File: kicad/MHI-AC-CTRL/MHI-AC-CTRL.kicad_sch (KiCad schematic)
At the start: 9 parts, among them J1 Conn_01x05, J3 Conn_01x03, U1 TSR_1-2450, U2 WeMos_D1_mini, U3 LEVEL-SHIFTER-4CH

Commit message: KiCad: Fix J1 connector (#155)
This fixes the J1 connector footprint and 3D model by using
easyeda2kicad [0] to pull the data from LCSC!

Closes #111

[0]: https://github.com/uPesy/easyeda2kicad.py

Signed-off-by: Olliver Schinagl <oliver@schinagl.nl>
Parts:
- J1: footprint Connector_JST:JST_XH_B5B-XH-A_1x05_P2.50mm_Vertical -> easyeda2kicad:CONN-TH_5P-P2.50_05JQ-BT

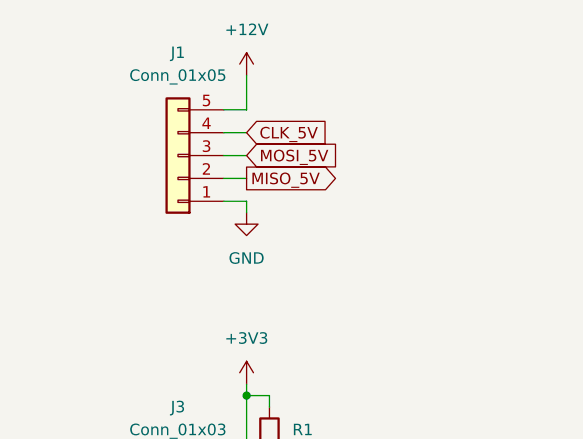
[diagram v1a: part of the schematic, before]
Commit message: Correct J1 connector pinout (#168)
Fixes #167
Regenerated PDF and gerber/drill
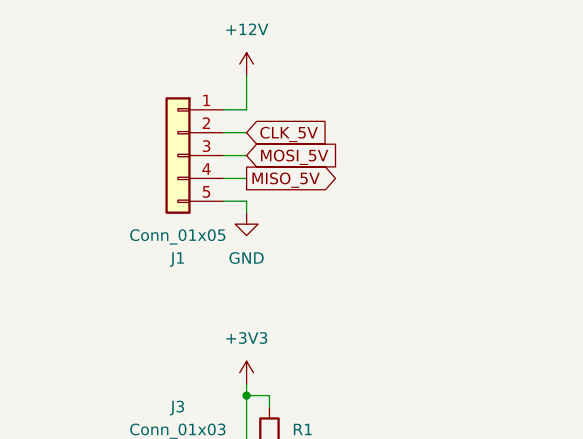
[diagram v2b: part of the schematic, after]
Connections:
- net +12V: now also J1.1 (Pin_1); no longer J1.5 (Pin_5)
- net CLK_5V: now also J1.2 (Pin_2); no longer J1.4 (Pin_4)
- net GND: now also J1.5 (Pin_5); no longer J1.1 (Pin_1)
- net MISO_5V: now also J1.4 (Pin_4); no longer J1.2 (Pin_2)
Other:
- moved on the sheet: J1
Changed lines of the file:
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@@
   (no_connect (at 111.76 54.61))
   (no_connect (at 111.76 44.45))
+  (wire (pts (xy 40.64 39.37) (xy 43.18 39.37))
+    (stroke (width 0) (type default))
+  )
   (wire (pts (xy 109.22 46.99) (xy 111.76 46.99))
     (stroke (width 0) (type default))
@@
     (stroke (width 0) (type default))
   )
+  (wire (pts (xy 40.64 44.45) (xy 43.18 44.45))
+    (stroke (width 0) (type default))
+  )
+  (wire (pts (xy 40.64 76.2) (xy 45.72 76.2))
+    (stroke (width 0) (type default))
+  )
+  (wire (pts (xy 158.75 62.23) (xy 156.21 62.23))
+    (stroke (width 0) (type default))
+  )
+  (wire (pts (xy 109.22 49.53) (xy 111.76 49.53))
+    (stroke (width 0) (type default))
+  )
+  (wire (pts (xy 109.22 54.61) (xy 111.76 54.61))
+    (stroke (width 0) (type default))
+  )
+  (wire (pts (xy 86.36 46.99) (xy 88.9 46.99))
+    (stroke (width 0) (type default))
+  )
+  (wire (pts (xy 158.75 52.07) (xy 156.21 52.07))
+    (stroke (width 0) (type default))
+  )
+  (wire (pts (xy 109.22 57.15) (xy 111.76 57.15))
+    (stroke (width 0) (type default))
+  )
+  (wire (pts (xy 31.75 111.76) (xy 31.75 110.49))
+    (stroke (width 0) (type default))
+  )
+  (wire (pts (xy 109.22 62.23) (xy 111.76 62.23))
+    (stroke (width 0) (type default))
+  )
+  (wire (pts (xy 43.18 73.66) (xy 43.18 66.04))
+    (stroke (width 0) (type default))
+  )
+  (wire (pts (xy 31.75 101.6) (xy 31.75 110.49))
+    (stroke (width 0) (type default))
+  )
+  (wire (pts (xy 40.64 73.66) (xy 43.18 73.66))
+    (stroke (width 0) (type default))
+  )
+  (wire (pts (xy 43.18 78.74) (xy 43.18 80.01))
+    (stroke (width 0) (type default))
+  )
+  (wire (pts (xy 109.22 64.77) (xy 111.76 64.77))
+    (stroke (width 0) (type default))
+  )
+  (wire (pts (xy 158.75 57.15) (xy 156.21 57.15))
+    (stroke (width 0) (type default))
+  )
+  (wire (pts (xy 38.1 119.38) (xy 38.1 120.65))
+    (stroke (width 0) (type default))
+  )
+  (wire (pts (xy 40.64 41.91) (xy 43.18 41.91))
+    (stroke (width 0) (type default))
+  )
+  (wire (pts (xy 171.45 77.47) (xy 171.45 80.01))
+    (stroke (width 0) (type default))
+  )
+  (wire (pts (xy 99.06 77.47) (xy 99.06 80.01))
+    (stroke (width 0) (type default))
+  )
+  (wire (pts (xy 40.64 78.74) (xy 43.18 78.74))
+    (stroke (width 0) (type default))
+  )
+  (wire (pts (xy 43.18 66.04) (xy 43.18 64.77))
+    (stroke (width 0) (type default))
+  )
+  (wire (pts (xy 43.18 110.49) (xy 38.1 110.49))
+    (stroke (width 0) (type default))
+  )
+  (wire (pts (xy 53.34 118.11) (xy 53.34 120.65))
+    (stroke (width 0) (type default))
+  )
+  (wire (pts (xy 45.72 66.04) (xy 43.18 66.04))
+    (stroke (width 0) (type default))
+  )
+  (wire (pts (xy 109.22 52.07) (xy 111.76 52.07))
+    (stroke (width 0) (type default))
+  )
+  (wire (pts (xy 45.72 76.2) (xy 48.26 76.2))
+    (stroke (width 0) (type default))
+  )
+  (wire (pts (xy 67.31 119.38) (xy 67.31 120.65))
+    (stroke (width 0) (type default))
+  )
+  (wire (pts (xy 109.22 59.69) (xy 111.76 59.69))
+    (stroke (width 0) (type default))
+  )
+  (wire (pts (xy 179.07 62.23) (xy 181.61 62.23))
+    (stroke (width 0) (type default))
+  )
+  (wire (pts (xy 43.18 34.29) (xy 43.18 30.48))
+    (stroke (width 0) (type default))
+  )
+  (wire (pts (xy 179.07 52.07) (xy 181.61 52.07))
+    (stroke (width 0) (type default))
+  )
+  (wire (pts (xy 166.37 77.47) (xy 166.37 80.01))
+    (stroke (width 0) (type default))
+  )
   (wire (pts (xy 40.64 34.29) (xy 43.18 34.29))
     (stroke (width 0) (type default))
   )
-  (wire (pts (xy 40.64 76.2) (xy 45.72 76.2))
-    (stroke (width 0) (type default))
-  )
-  (wire (pts (xy 158.75 62.23) (xy 156.21 62.23))
-    (stroke (width 0) (type default))
-  )
-  (wire (pts (xy 109.22 49.53) (xy 111.76 49.53))
-    (stroke (width 0) (type default))
-  )
-  (wire (pts (xy 40.64 41.91) (xy 43.18 41.91))
-    (stroke (width 0) (type default))
-  )
-  (wire (pts (xy 109.22 54.61) (xy 111.76 54.61))
-    (stroke (width 0) (type default))
-  )
-  (wire (pts (xy 86.36 46.99) (xy 88.9 46.99))
-    (stroke (width 0) (type default))
-  )
-  (wire (pts (xy 158.75 52.07) (xy 156.21 52.07))
-    (stroke (width 0) (type default))
-  )
-  (wire (pts (xy 109.22 57.15) (xy 111.76 57.15))
-    (stroke (width 0) (type default))
-  )
-  (wire (pts (xy 31.75 111.76) (xy 31.75 110.49))
-    (stroke (width 0) (type default))
-  )
-  (wire (pts (xy 109.22 62.23) (xy 111.76 62.23))
-    (stroke (width 0) (type default))
-  )
-  (wire (pts (xy 43.18 73.66) (xy 43.18 66.04))
-    (stroke (width 0) (type default))
-  )
-  (wire (pts (xy 31.75 101.6) (xy 31.75 110.49))
-    (stroke (width 0) (type default))
-  )
-  (wire (pts (xy 40.64 73.66) (xy 43.18 73.66))
-    (stroke (width 0) (type default))
-  )
-  (wire (pts (xy 43.18 78.74) (xy 43.18 80.01))
-    (stroke (width 0) (type default))
-  )
-  (wire (pts (xy 109.22 64.77) (xy 111.76 64.77))
-    (stroke (width 0) (type default))
-  )
-  (wire (pts (xy 158.75 57.15) (xy 156.21 57.15))
-    (stroke (width 0) (type default))
-  )
-  (wire (pts (xy 40.64 44.45) (xy 43.18 44.45))
-    (stroke (width 0) (type default))
-  )
-  (wire (pts (xy 38.1 119.38) (xy 38.1 120.65))
-    (stroke (width 0) (type default))
-  )
-  (wire (pts (xy 40.64 39.37) (xy 43.18 39.37))
-    (stroke (width 0) (type default))
-  )
-  (wire (pts (xy 171.45 77.47) (xy 171.45 80.01))
-    (stroke (width 0) (type default))
-  )
-  (wire (pts (xy 99.06 77.47) (xy 99.06 80.01))
-    (stroke (width 0) (type default))
-  )
-  (wire (pts (xy 40.64 78.74) (xy 43.18 78.74))
+  (wire (pts (xy 96.52 31.75) (xy 96.52 36.83))
     (stroke (width 0) (type default))
   )
   (wire (pts (xy 40.64 36.83) (xy 43.18 36.83))
-    (stroke (width 0) (type default))
-  )
-  (wire (pts (xy 43.18 66.04) (xy 43.18 64.77))
-    (stroke (width 0) (type default))
-  )
-  (wire (pts (xy 43.18 110.49) (xy 38.1 110.49))
-    (stroke (width 0) (type default))
-  )
-  (wire (pts (xy 53.34 118.11) (xy 53.34 120.65))
-    (stroke (width 0) (type default))
-  )
-  (wire (pts (xy 45.72 66.04) (xy 43.18 66.04))
-    (stroke (width 0) (type default))
-  )
-  (wire (pts (xy 109.22 52.07) (xy 111.76 52.07))
-    (stroke (width 0) (type default))
-  )
-  (wire (pts (xy 45.72 76.2) (xy 48.26 76.2))
-    (stroke (width 0) (type default))
-  )
-  (wire (pts (xy 67.31 119.38) (xy 67.31 120.65))
-    (stroke (width 0) (type default))
-  )
-  (wire (pts (xy 109.22 59.69) (xy 111.76 59.69))
-    (stroke (width 0) (type default))
-  )
-  (wire (pts (xy 179.07 62.23) (xy 181.61 62.23))
-    (stroke (width 0) (type default))
-  )
-  (wire (pts (xy 43.18 34.29) (xy 43.18 30.48))
-    (stroke (width 0) (type default))
-  )
-  (wire (pts (xy 179.07 52.07) (xy 181.61 52.07))
-    (stroke (width 0) (type default))
-  )
-  (wire (pts (xy 166.37 77.47) (xy 166.37 80.01))
-    (stroke (width 0) (type default))
-  )
-  (wire (pts (xy 96.52 31.75) (xy 96.52 36.83))
     (stroke (width 0) (type default))
   )
@@
     )
   )
-  (symbol (lib_id "Connector_Generic:Conn_01x05") (at 35.56 39.37 180) (unit 1)
-    (in_bom yes) (on_board yes) (dnp no) (fields_autoplaced)
-    (property "Reference" "J1" (at 35.56 27.94 0)
-      (effects (font (size 1.27 1.27)))
-    )
-    (property "Value" "Conn_01x05" (at 35.56 30.48 0)
-      (effects (font (size 1.27 1.27)))
-    )
+  (symbol (lib_id "Connector_Generic:Conn_01x05") (at 35.56 39.37 0) (mirror y) (unit 1)
+    (in_bom yes) (on_board yes) (dnp no)
+    (property "Reference" "J1" (at 35.56 50.8 0)
+      (effects (font (size 1.27 1.27)))
+    )
+    (property "Value" "Conn_01x05" (at 35.56 48.26 0)
+      (effects (font (size 1.27 1.27)))
+    )
